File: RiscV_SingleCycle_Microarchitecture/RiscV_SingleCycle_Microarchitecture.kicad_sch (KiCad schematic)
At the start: 20 parts

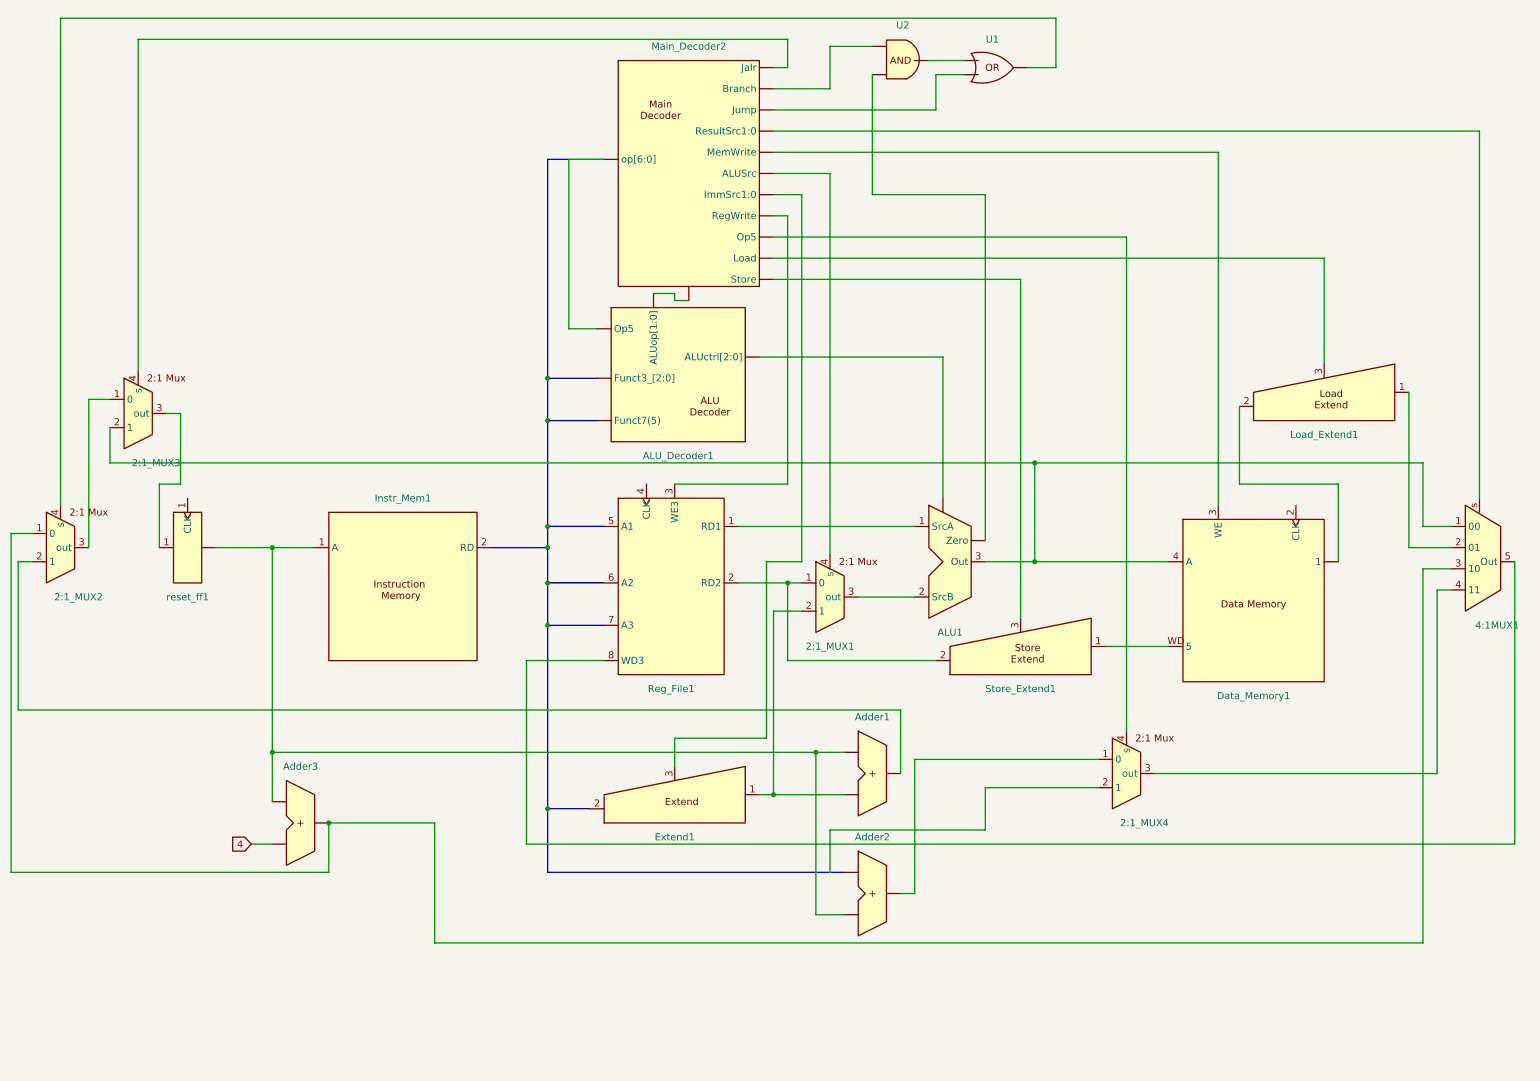
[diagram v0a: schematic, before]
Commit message: fix: riscv cpu with testbench for whole rv32i ISA
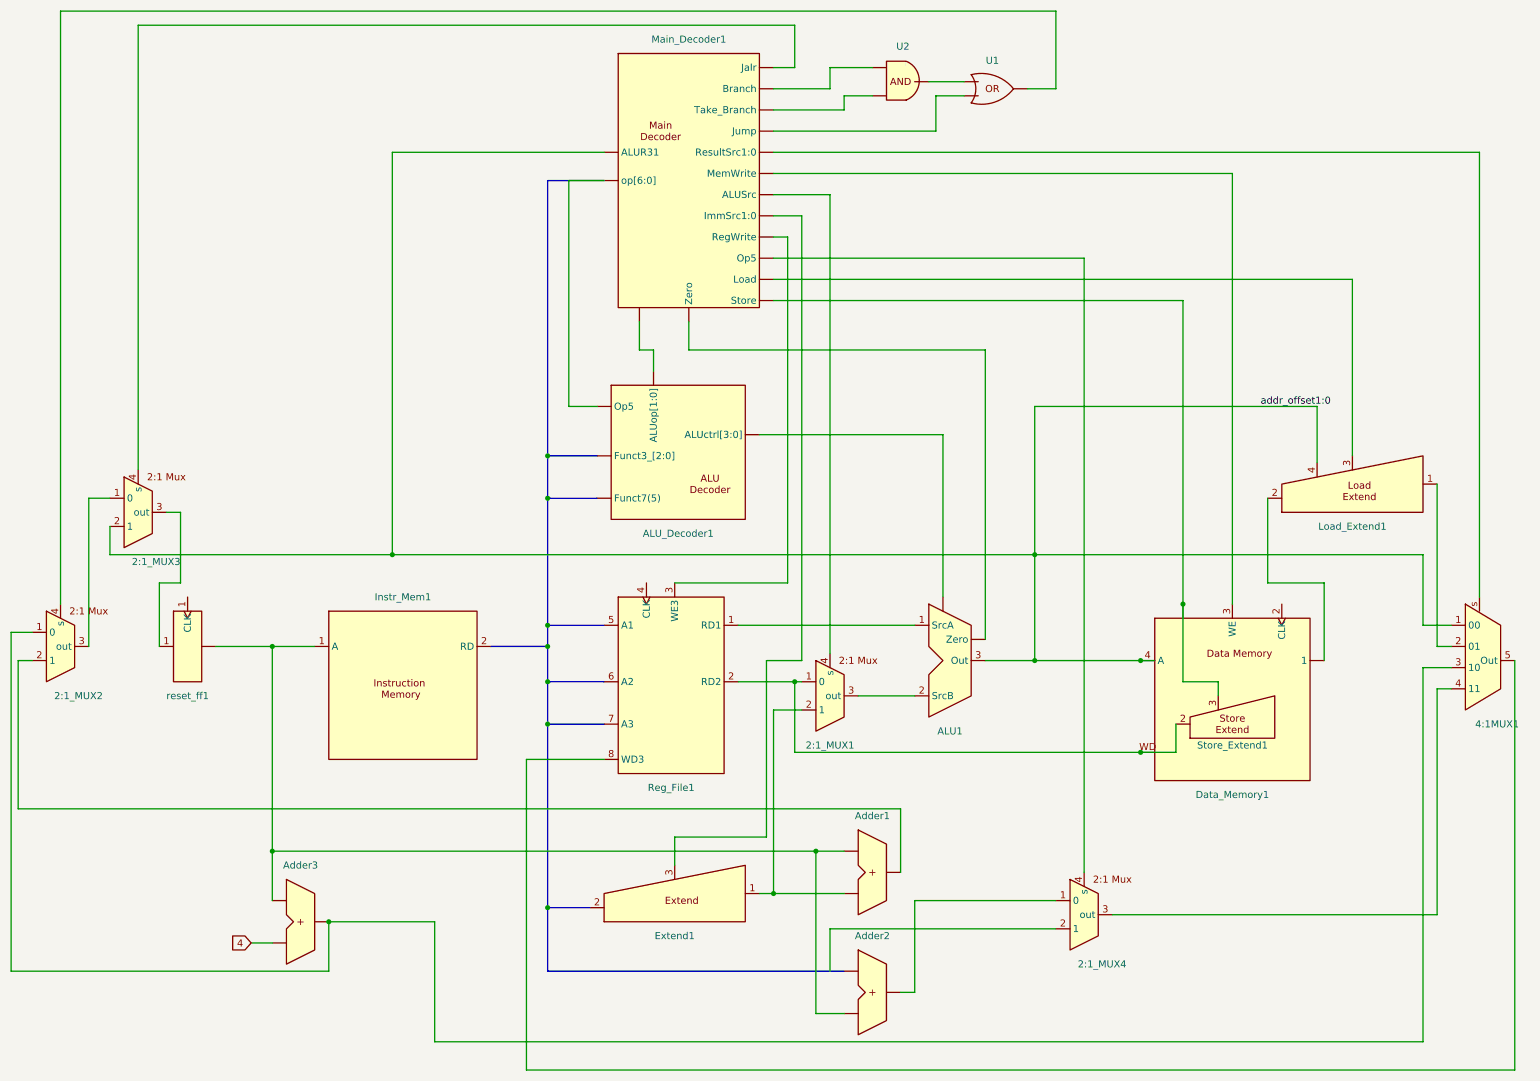
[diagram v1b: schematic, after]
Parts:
- removed Main_Decoder2: ~, symbol RiscV_Microachitecture:Main_Decoder
- added Main_Decoder1: ~, symbol RiscV_Microachitecture:Main_Decoder
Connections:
- net addr_offset1:0: now reaches 2:1_MUX3.2 (1), 4:1MUX1.1 (00), ALU1.3 (Out), Data_Memory1.4 (A)
- net addr_offset1:0: now also Load_Extend1.4, Main_Decoder1. (op[6:0])
- net at 4:1MUX1.s: now also Main_Decoder1. (op[6:0])
- net at Adder2.: now also Adder1., Adder3., Instr_Mem1.1 (A), reset_ff1.
- net at ALU1. (Zero): now also ALU_Decoder1. (Op5); no longer U2.
- net at Data_Memory1.WD: now also 2:1_MUX1.1 (0), Reg_File1.2 (RD2), Store_Extend1.2; no longer Store_Extend1.1
- net at Store_Extend1.3: now also Data_Memory1. (1), Main_Decoder1. (op[6:0])
- net at 2:1_MUX4.4 (s): now also Main_Decoder1. (op[6:0])
- net at Data_Memory1.3 (WE): now also Main_Decoder1. (op[6:0])
- net at reset_ff1.1 (CLK): now also 2:1_MUX3.3 (out)
- net at 2:1_MUX1.4 (s): now also Main_Decoder1. (op[6:0])
- net at Reg_File1.3 (WE3): now also Main_Decoder1. (op[6:0])
- net at Extend1.3: now also Main_Decoder1. (op[6:0])
- net at Load_Extend1.3: now also Main_Decoder1. (op[6:0])
- net at 2:1_MUX3.4 (s): now also Main_Decoder1. (op[6:0])
- new net: ALU_Decoder1. (Op5), Main_Decoder1. (op[6:0]) (x2)
- new net: ALU1. (Zero), Main_Decoder1. (op[6:0])
- new net: Main_Decoder1. (op[6:0]), U2. (x2)
- new net: Main_Decoder1. (op[6:0]), U1.
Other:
- moved on the sheet: 2:1_MUX1, 2:1_MUX2, 2:1_MUX3, 2:1_MUX4, 4:1MUX1, ALU1, Adder1, Adder2, Adder3, Extend1, Instr_Mem1, Reg_File1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
